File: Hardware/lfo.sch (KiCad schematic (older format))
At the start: 32 parts, among them Q5 2N3904, Q6 2N3904, Q7 2N3904, Q8 2N3904

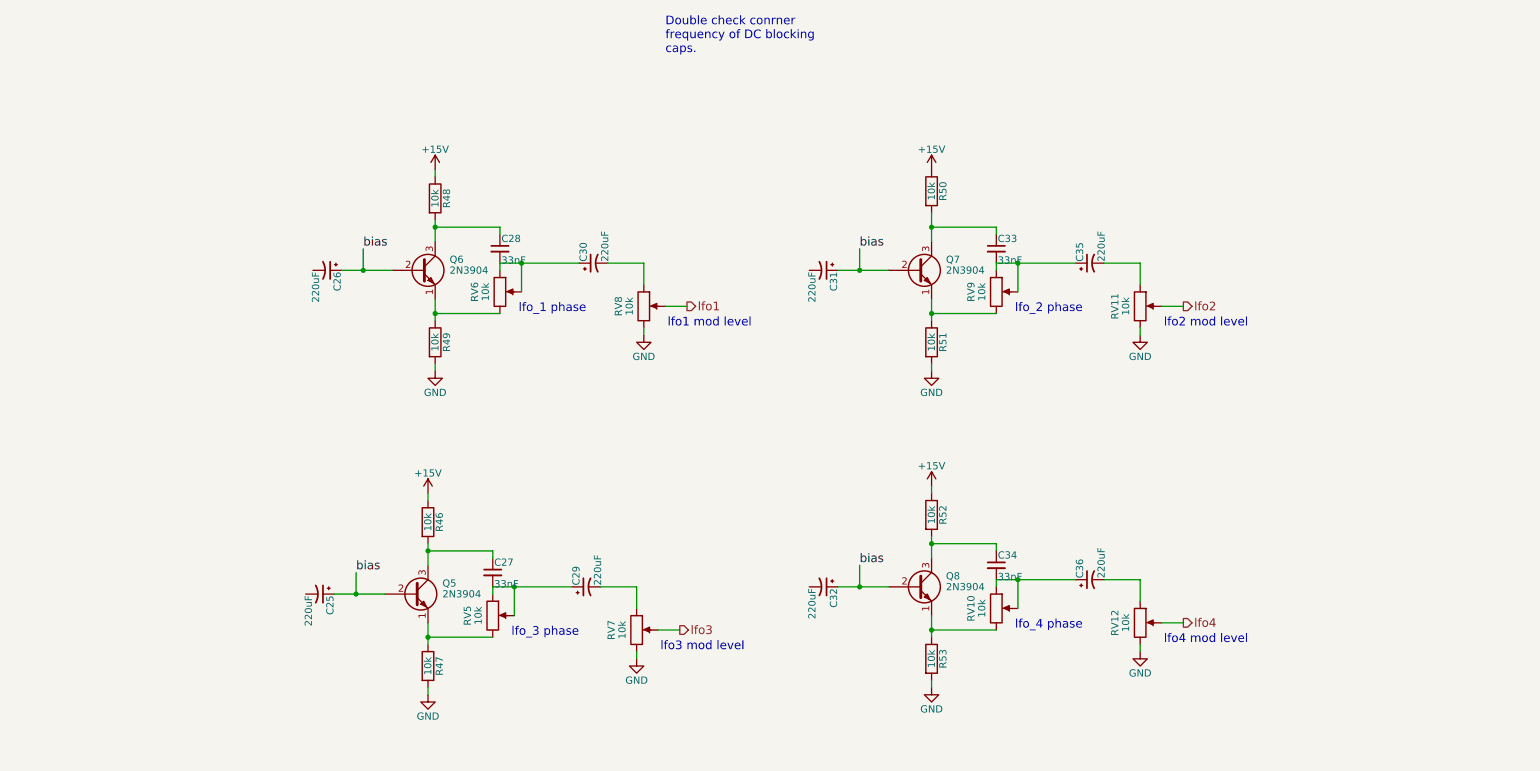
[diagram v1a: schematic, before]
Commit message: change corner frequency of DC blocking caps  everywhere they are in use.  Updated some simulation files to test filter circuits.
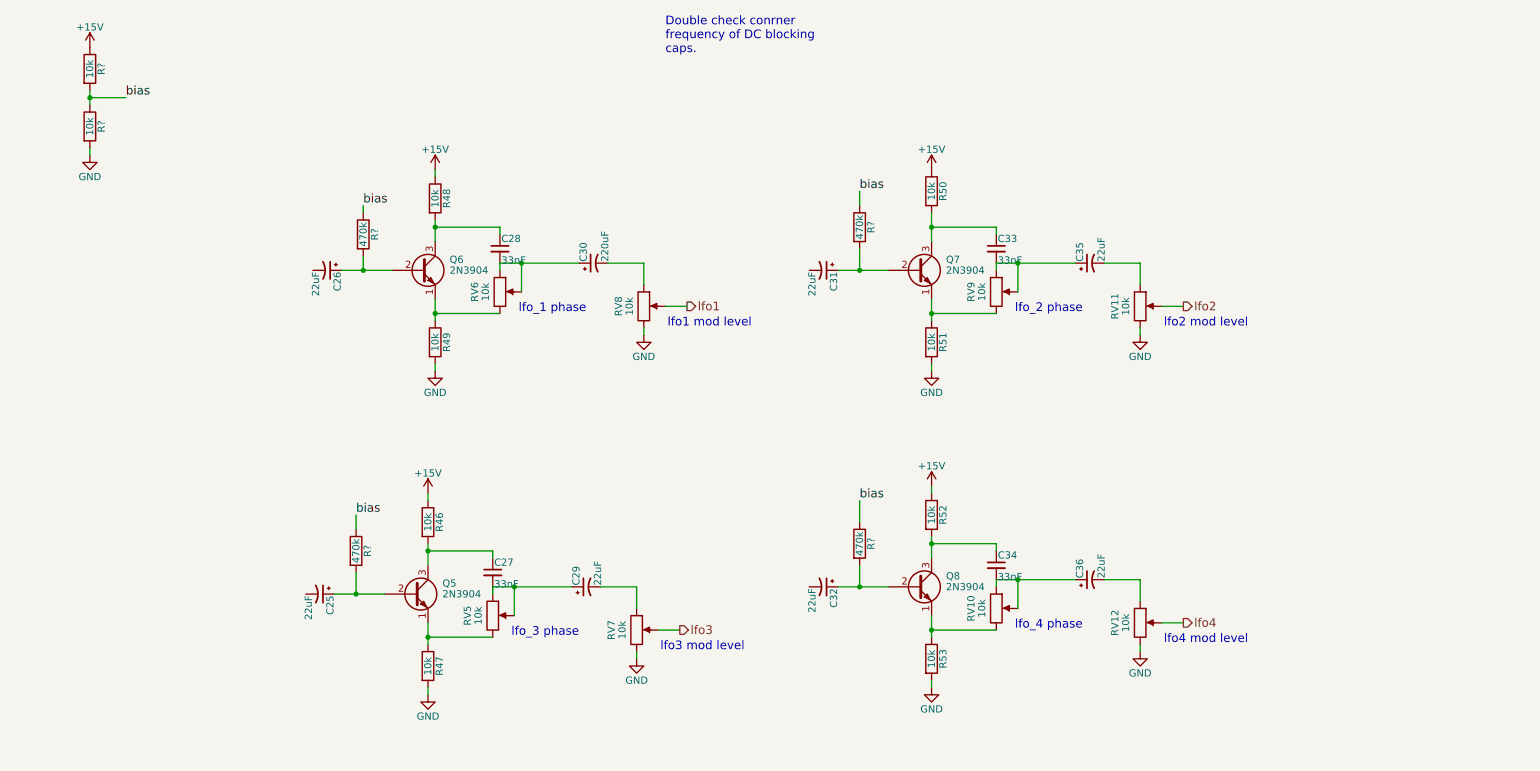
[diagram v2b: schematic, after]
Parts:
- added R? (x2): 10k, symbol R
- added R? (x4): 470k, symbol R
- C25, C26, C29, C31, C32, C35, C36: value 220uF -> 22uF
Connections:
- net +15V: now also R?.1
- net GND: now also R?.2
- net bias: now also R?.1, R?.1, R?.1, R?.1, R?.1, R?.2; no longer C25.1, C26.1, C31.1, C32.1, Q5.2 (B), Q6.2 (B), Q7.2 (B), Q8.2 (B)
- new net: C26.1, Q6.2 (B), R?.2
- new net: C31.1, Q7.2 (B), R?.2
- new net: C25.1, Q5.2 (B), R?.2
- new net: C32.1, Q8.2 (B), R?.2
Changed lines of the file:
@@
 	1    0    0    -1
 $EndComp
-Text Label 2950 2400 0    60   ~ 0
+Text Label 2950 2100 0    60   ~ 0
 bias
 $Comp
@@
 Connection ~ 3450 2850
 Connection ~ 4050 2500
-Wire Wire Line
-	2950 2400 2950 2550
 Connection ~ 2950 2550
 $Comp
@@
 P 2700 2550
 F 0 "C26" H 2710 2620 50  0000 L CNN
-F 1 "220uF" H 2710 2470 50  0000 L CNN
+F 1 "22uF" H 2710 2470 50  0000 L CNN
 F 2 "" H 2700 2550 50  0001 C CNN
 F 3 "" H 2700 2550 50  0001 C CNN
@@
 	1    0    0    -1
 $EndComp
-Text Label 6400 2400 0    60   ~ 0
+Text Label 6400 2000 0    60   ~ 0
 bias
 $Comp
@@
 P 6150 2550
 F 0 "C31" H 6160 2620 50  0000 L CNN
-F 1 "220uF" H 6160 2470 50  0000 L CNN
+F 1 "22uF" H 6160 2470 50  0000 L CNN
 F 2 "" H 6150 2550 50  0001 C CNN
 F 3 "" H 6150 2550 50  0001 C CNN
@@
 P 8000 2500
 F 0 "C35" H 8010 2570 50  0000 L CNN
-F 1 "220uF" H 8010 2420 50  0000 L CNN
+F 1 "22uF" H 8010 2420 50  0000 L CNN
 F 2 "" H 8000 2500 50  0001 C CNN
 F 3 "" H 8000 2500 50  0001 C CNN
@@
 	1    0    0    -1
 $EndComp
-Text Label 2900 4650 0    60   ~ 0
+Text Label 2900 4250 0    60   ~ 0
 bias
 $Comp
@@
 P 2650 4800
 F 0 "C25" H 2660 4870 50  0000 L CNN
-F 1 "220uF" H 2660 4720 50  0000 L CNN
+F 1 "22uF" H 2660 4720 50  0000 L CNN
 F 2 "" H 2650 4800 50  0001 C CNN
 F 3 "" H 2650 4800 50  0001 C CNN
@@
 P 4500 4750
 F 0 "C29" H 4510 4820 50  0000 L CNN
-F 1 "220uF" H 4510 4670 50  0000 L CNN
+F 1 "22uF" H 4510 4670 50  0000 L CNN
 F 2 "" H 4500 4750 50  0001 C CNN
 F 3 "" H 4500 4750 50  0001 C CNN
@@
 	1    0    0    -1
 $EndComp
-Text Label 6400 4600 0    60   ~ 0
+Text Label 6400 4150 0    60   ~ 0
 bias
 $Comp
@@
 P 6150 4750
 F 0 "C32" H 6160 4820 50  0000 L CNN
-F 1 "220uF" H 6160 4670 50  0000 L CNN
+F 1 "22uF" H 6160 4670 50  0000 L CNN
 F 2 "" H 6150 4750 50  0001 C CNN
 F 3 "" H 6150 4750 50  0001 C CNN
@@
 P 8000 4700
 F 0 "C36" H 8010 4770 50  0000 L CNN
-F 1 "220uF" H 8010 4620 50  0000 L CNN
+F 1 "22uF" H 8010 4620 50  0000 L CNN
 F 2 "" H 8000 4700 50  0001 C CNN
 F 3 "" H 8000 4700 50  0001 C CNN
@@
 Text Notes 9100 5150 2    60   ~ 0
 lfo4 mod level
+$Comp
+L +15V #PWR?
+U 1 1 5C37F050
+P 1050 1000
+F 0 "#PWR?" H 1050 850 50  0001 C CNN
+F 1 "+15V" H 1050 1140 50  0000 C CNN
+F 2 "" H 1050 1000 50  0001 C CNN
+F 3 "" H 1050 1000 50  0001 C CNN
+	1    1050 1000
+	1    0    0    -1
+$EndComp
+$Comp
+L R R?
+U 1 1 5C37F0DB
+P 1050 1150
+F 0 "R?" V 1130 1150 50  0000 C CNN
+F 1 "10k" V 1050 1150 50  0000 C CNN
+F 2 "" V 980 1150 50  0001 C CNN
+F 3 "" H 1050 1150 50  0001 C CNN
+	1    1050 1150
+	1    0    0    -1
+$EndComp
+$Comp
+L R R?
+U 1 1 5C37F1BF
+P 1050 1550
+F 0 "R?" V 1130 1550 50  0000 C CNN
+F 1 "10k" V 1050 1550 50  0000 C CNN
+F 2 "" V 980 1550 50  0001 C CNN
+F 3 "" H 1050 1550 50  0001 C CNN
+	1    1050 1550
+	1    0    0    -1
+$EndComp
+$Comp
+L GND #PWR?
+U 1 1 5C37F24D
+P 1050 1750
+F 0 "#PWR?" H 1050 1500 50  0001 C CNN
+F 1 "GND" H 1050 1600 50  0000 C CNN
+F 2 "" H 1050 1750 50  0001 C CNN
+F 3 "" H 1050 1750 50  0001 C CNN
+	1    1050 1750
+	1    0    0    -1
+$EndComp
+Wire Wire Line
+	1050 1750 1050 1700
+Wire Wire Line
+	1050 1300 1050 1400
+Text Label 1300 1350 0    60   ~ 0
+bias
+Wire Wire Line
+	1300 1350 1050 1350
+Connection ~ 1050 1350
+$Comp
+L R R?
+U 1 1 5C37F4DB
+P 2950 2300
+F 0 "R?" V 3030 2300 50  0000 C CNN
+F 1 "470k" V 2950 2300 50  0000 C CNN
+F 2 "" V 2880 2300 50  0001 C CNN
+F 3 "" H 2950 2300 50  0001 C CNN
+	1    2950 2300
+	1    0    0    -1
+$EndComp
+Wire Wire Line
+	2950 2100 2950 2150
+Wire Wire Line
+	2950 2450 2950 2550
+$Comp
+L R R?
+U 1 1 5C37F889
+P 2900 4500
+F 0 "R?" V 2980 4500 50  0000 C CNN
+F 1 "470k" V 2900 4500 50  0000 C CNN
+F 2 "" V 2830 4500 50  0001 C CNN
+F 3 "" H 2900 4500 50  0001 C CNN
+	1    2900 4500
+	1    0    0    -1
+$EndComp
+$Comp
+L R R?
+U 1 1 5C37F945
+P 6400 2250
+F 0 "R?" V 6480 2250 50  0000 C CNN
+F 1 "470k" V 6400 2250 50  0000 C CNN
+F 2 "" V 6330 2250 50  0001 C CNN
+F 3 "" H 6400 2250 50  0001 C CNN
+	1    6400 2250
+	1    0    0    -1
+$EndComp
+$Comp
+L R R?
+U 1 1 5C37FA46
+P 6400 4450
+F 0 "R?" V 6480 4450 50  0000 C CNN
+F 1 "470k" V 6400 4450 50  0000 C CNN
+F 2 "" V 6330 4450 50  0001 C CNN
+F 3 "" H 6400 4450 50  0001 C CNN
+	1    6400 4450
+	1    0    0    -1
+$EndComp
+Wire Wire Line
+	2900 4250 2900 4350
+Wire Wire Line
+	6400 2000 6400 2100
+Wire Wire Line
+	6400 4300 6400 4150
 $EndSCHEMATC

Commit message: add analog LFO to schematic
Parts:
- added C?: 22uF, symbol CP1
- added C?: 220uF, symbol CP1
- added R?: 10k, symbol R
- added R?: 470, symbol R
- added R?: 2.2k, symbol R
- added R? (x2): 470k, symbol R
- added R?: 100k, symbol R
- added RV?: 10k, symbol POT
- added U? (x2): TL072, symbol TL072
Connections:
- net +15V: now also U?.8 (V+), U?.8 (V+)
- net GND: now also R?.1, U?.4 (V-), U?.4 (V-)
- net main_lfo: now reaches C26.2
- net main_lfo: now also C25.2, C31.2, C32.2, C?.2, R?.2
- new net: R?.1, R?.2, U?.1
- new net: R?.1, U?.2 (-)
- new net: R?.2, R?.2, U?.3 (+)
- new net: C?.1, C?.2, R?.1, U?.1
- new net: C?.1, RV?.1, RV?.2, U?.2 (-)
- new net: R?.1, U?.3 (+)
- new net: R?.1, RV?.3
- new net VREF: R?.2, R?.2
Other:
- moved on the sheet: C25, C26, C27, C28, C29, C30, C31, C32, C33, C34, C35, C36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

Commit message: begin to add taper to potentiometers. I think they're all right, but some tapers may change under test.
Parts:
- RV10, RV5, RV6, RV9: value 10k -> 10kB
- RV11, RV12, RV7, RV8, RV?: value 10k -> 10kA
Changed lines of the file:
@@
 P 5850 2950
 F 0 "RV6" V 5675 2950 50  0000 C CNN
-F 1 "10k" V 5750 2950 50  0000 C CNN
+F 1 "10kB" V 5750 2950 50  0000 C CNN
 F 2 "" H 5850 2950 50  0001 C CNN
 F 3 "" H 5850 2950 50  0001 C CNN
@@
 P 6850 3050
 F 0 "RV8" V 6675 3050 50  0000 C CNN
-F 1 "10k" V 6750 3050 50  0000 C CNN
+F 1 "10kA" V 6750 3050 50  0000 C CNN
 F 2 "" H 6850 3050 50  0001 C CNN
 F 3 "" H 6850 3050 50  0001 C CNN
@@
 P 9300 2950
 F 0 "RV9" V 9125 2950 50  0000 C CNN
-F 1 "10k" V 9200 2950 50  0000 C CNN
+F 1 "10kB" V 9200 2950 50  0000 C CNN
 F 2 "" H 9300 2950 50  0001 C CNN
 F 3 "" H 9300 2950 50  0001 C CNN
@@
 P 10300 3050
 F 0 "RV11" V 10125 3050 50  0000 C CNN
-F 1 "10k" V 10200 3050 50  0000 C CNN
+F 1 "10kA" V 10200 3050 50  0000 C CNN
 F 2 "" H 10300 3050 50  0001 C CNN
 F 3 "" H 10300 3050 50  0001 C CNN
@@
 P 5800 5200
 F 0 "RV5" V 5625 5200 50  0000 C CNN
-F 1 "10k" V 5700 5200 50  0000 C CNN
+F 1 "10kB" V 5700 5200 50  0000 C CNN
 F 2 "" H 5800 5200 50  0001 C CNN
 F 3 "" H 5800 5200 50  0001 C CNN
@@
 P 6800 5300
 F 0 "RV7" V 6625 5300 50  0000 C CNN
-F 1 "10k" V 6700 5300 50  0000 C CNN
+F 1 "10kA" V 6700 5300 50  0000 C CNN
 F 2 "" H 6800 5300 50  0001 C CNN
 F 3 "" H 6800 5300 50  0001 C CNN
@@
 P 9300 5150
 F 0 "RV10" V 9125 5150 50  0000 C CNN
-F 1 "10k" V 9200 5150 50  0000 C CNN
+F 1 "10kB" V 9200 5150 50  0000 C CNN
 F 2 "" H 9300 5150 50  0001 C CNN
 F 3 "" H 9300 5150 50  0001 C CNN
@@
 P 10300 5250
 F 0 "RV12" V 10125 5250 50  0000 C CNN
-F 1 "10k" V 10200 5250 50  0000 C CNN
+F 1 "10kA" V 10200 5250 50  0000 C CNN
 F 2 "" H 10300 5250 50  0001 C CNN
 F 3 "" H 10300 5250 50  0001 C CNN
@@
 P 2500 3600
 F 0 "RV?" V 2325 3600 50  0000 C CNN
-F 1 "10k" V 2400 3600 50  0000 C CNN
+F 1 "10kA" V 2400 3600 50  0000 C CNN
 F 2 "" H 2500 3600 50  0001 C CNN
 F 3 "" H 2500 3600 50  0001 C CNN

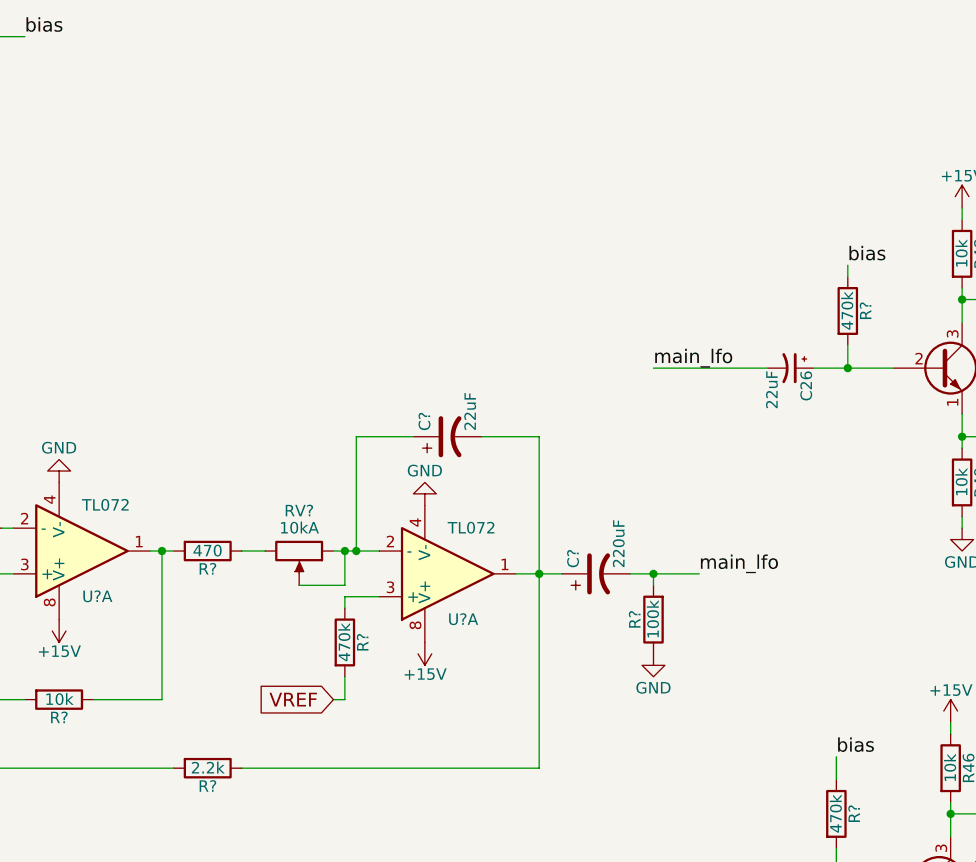
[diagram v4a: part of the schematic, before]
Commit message: add LFO waveshape selector switch
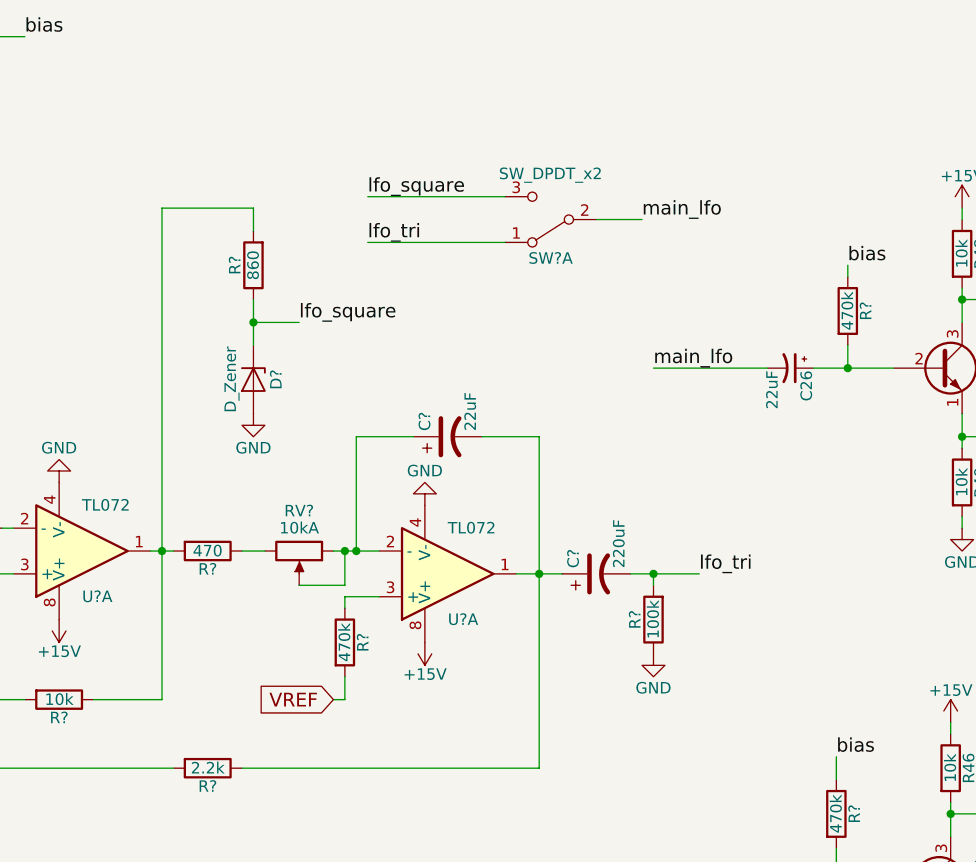
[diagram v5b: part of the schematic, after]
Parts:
- added D?: D_Zener, symbol D_Zener
- added R?: 860, symbol R
- added SW?: SW_DPDT_x2, symbol SW_DPDT_x2
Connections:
- net GND: now also D?.2 (A)
- net main_lfo: now also SW?.2 (B); no longer C?.2, R?.2
- net at R?.1, R?.2, U?.1: now also R?.2
- new net lfo_square: D?.1 (K), R?.1, SW?.3 (C)
- new net lfo_tri: C?.2, R?.2, SW?.1 (A)
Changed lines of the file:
@@
 	1    0    0    -1
 $EndComp
-Text Label 4250 3700 0    60   ~ 0
-main_lfo
 Text Label 4050 2800 0    60   ~ 0
 main_lfo
@@
 Text GLabel 2650 4250 0    60   Input ~ 0
 VREF
+$Comp
+L D_Zener D?
+U 1 1 5C38F192
+P 2300 2850
+F 0 "D?" H 2300 2950 50  0000 C CNN
+F 1 "D_Zener" H 2300 2750 50  0000 C CNN
+F 2 "" H 2300 2850 50  0001 C CNN
+F 3 "" H 2300 2850 50  0001 C CNN
+	1    2300 2850
+	0    1    1    0
+$EndComp
+$Comp
+L GND #PWR?
+U 1 1 5C38F259
+P 2300 3000
+F 0 "#PWR?" H 2300 2750 50  0001 C CNN
+F 1 "GND" H 2300 2850 50  0000 C CNN
+F 2 "" H 2300 3000 50  0001 C CNN
+F 3 "" H 2300 3000 50  0001 C CNN
+	1    2300 3000
+	-1   0    0    -1
+$EndComp
+$Comp
+L R R?
+U 1 1 5C38F2FA
+P 2300 2350
+F 0 "R?" V 2380 2350 50  0000 C CNN
+F 1 "860" V 2300 2350 50  0000 C CNN
+F 2 "" V 2230 2350 50  0001 C CNN
+F 3 "" H 2300 2350 50  0001 C CNN
+	1    2300 2350
+	-1   0    0    1
+$EndComp
 Wire Wire Line
 	4750 2800 5100 2800
@@
 	3000 3100 2750 3100
 Wire Wire Line
-	2750 3100 2750 3600
+	2750 3600 2750 3100
 Connection ~ 2750 3600
 Wire Wire Line
 	2700 3850 2700 3800
 Wire Wire Line
-	1900 3600 1900 4250
+	1900 2100 1900 4250
 Wire Wire Line
 	1900 4250 1600 4250
@@
 Wire Wire Line
 	2700 3800 2850 3800
+Wire Wire Line
+	2300 2500 2300 2700
+Wire Wire Line
+	1900 2100 2300 2100
+Wire Wire Line
+	2300 2100 2300 2200
+Text Label 2500 2600 0    60   ~ 0
+lfo_square
+Wire Wire Line
+	2500 2600 2300 2600
+Connection ~ 2300 2600
+Text Label 4250 3700 0    60   ~ 0
+lfo_tri
+$Comp
+L SW_DPDT_x2 SW?
+U 1 1 5C38FB5B
+P 3600 2150
+F 0 "SW?" H 3600 2320 50  0000 C CNN
+F 1 "SW_DPDT_x2" H 3600 1950 50  0000 C CNN
+F 2 "" H 3600 2150 50  0001 C CNN
+F 3 "" H 3600 2150 50  0001 C CNN
+	1    3600 2150
+	-1   0    0    1
+$EndComp
+Text Label 2800 2250 0    60   ~ 0
+lfo_tri
+Wire Wire Line
+	2800 2250 3400 2250
+Text Label 2800 2050 0    60   ~ 0
+lfo_square
+Wire Wire Line
+	2800 2050 3400 2050
+Text Label 4000 2150 0    60   ~ 0
+main_lfo
+Wire Wire Line
+	4000 2150 3800 2150
 $EndSCHEMATC

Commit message: mix LFO and Envelope drive signals instead of switching them, and add overall volume mix control to each channel.
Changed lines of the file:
@@
 	3000 3100 2750 3100
 Wire Wire Line
-	2750 3600 2750 3100
+	2750 3100 2750 3600
 Connection ~ 2750 3600
 Wire Wire Line
